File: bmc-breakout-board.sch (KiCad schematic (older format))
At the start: 26 parts, among them J1 PinHeader_2x4, J10 PinHeader_2x4, J11 PinHeader_2x05, J12 61300411121, J14 PCIE_BUS_x1, J15 0473460001, J16 PinHeader_1x07, J17 UE27AC54100, J2 PinHeader_2x13, J3 PinHeader_2x08, J4 61300411121, J5 ME1016813401101, J6 61300411121, J7 DC_SOCKET, J8 PinHeader_2x05, J9 PinHeader_1x07, Q1 BSS138AKA

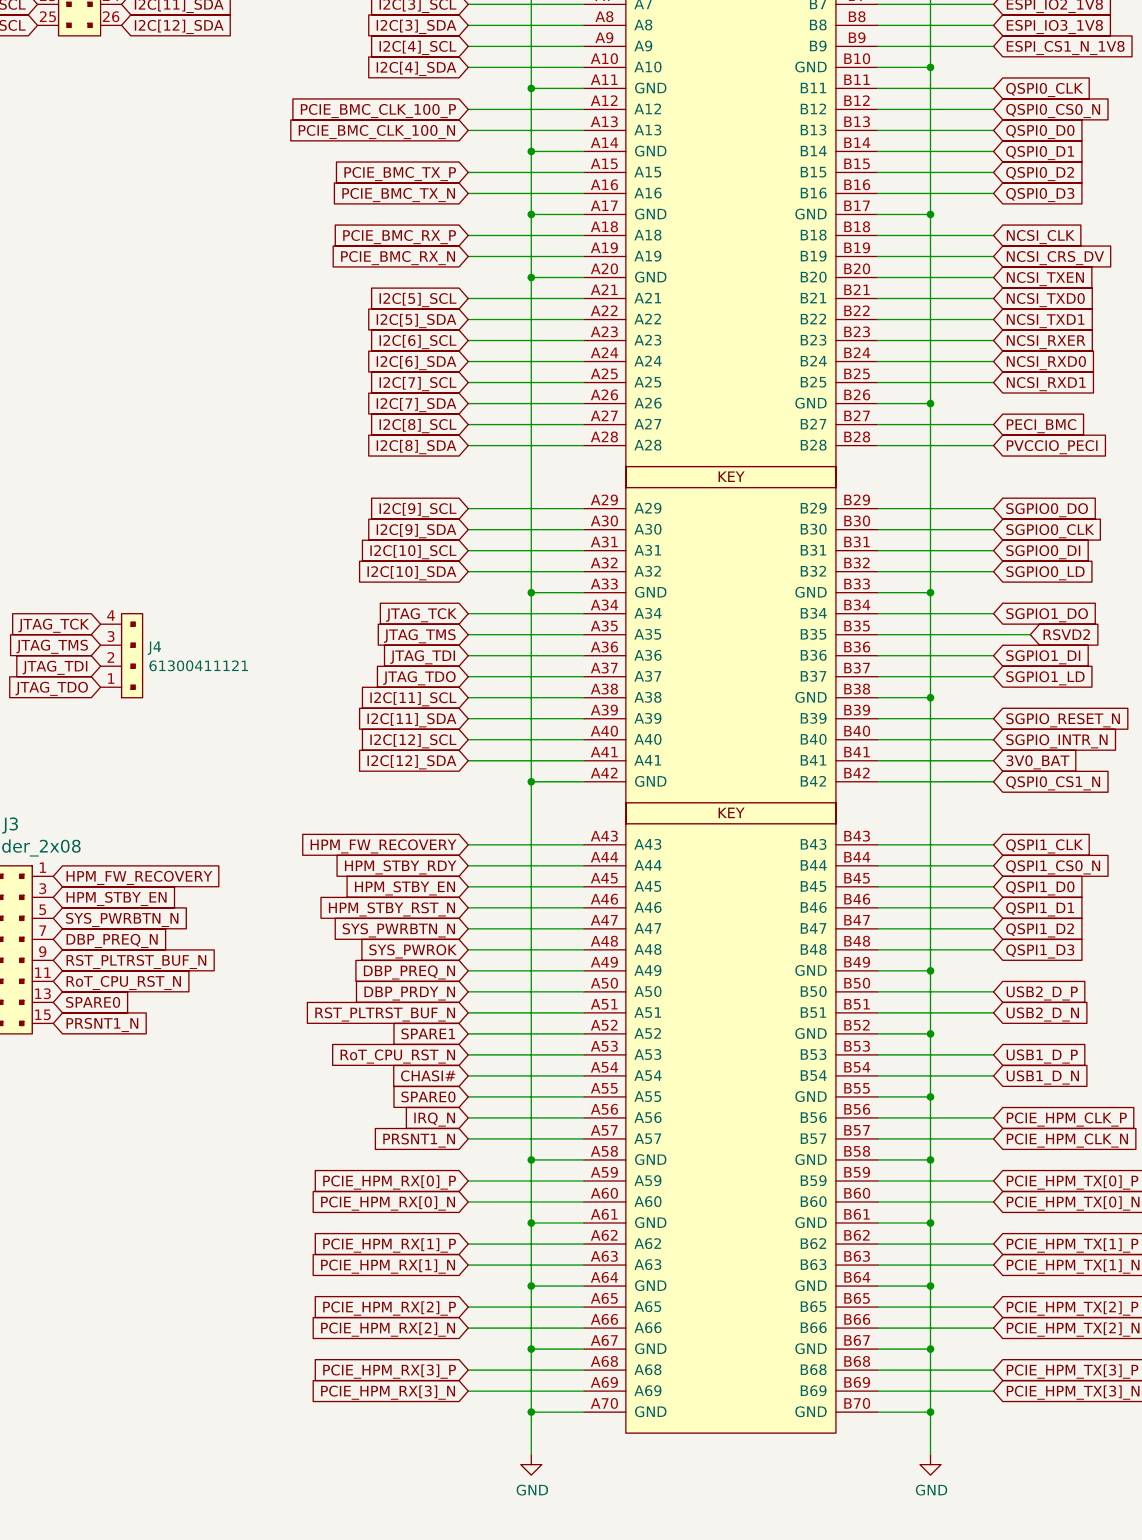
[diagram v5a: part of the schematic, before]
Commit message: Add decoupling on PCIe lines
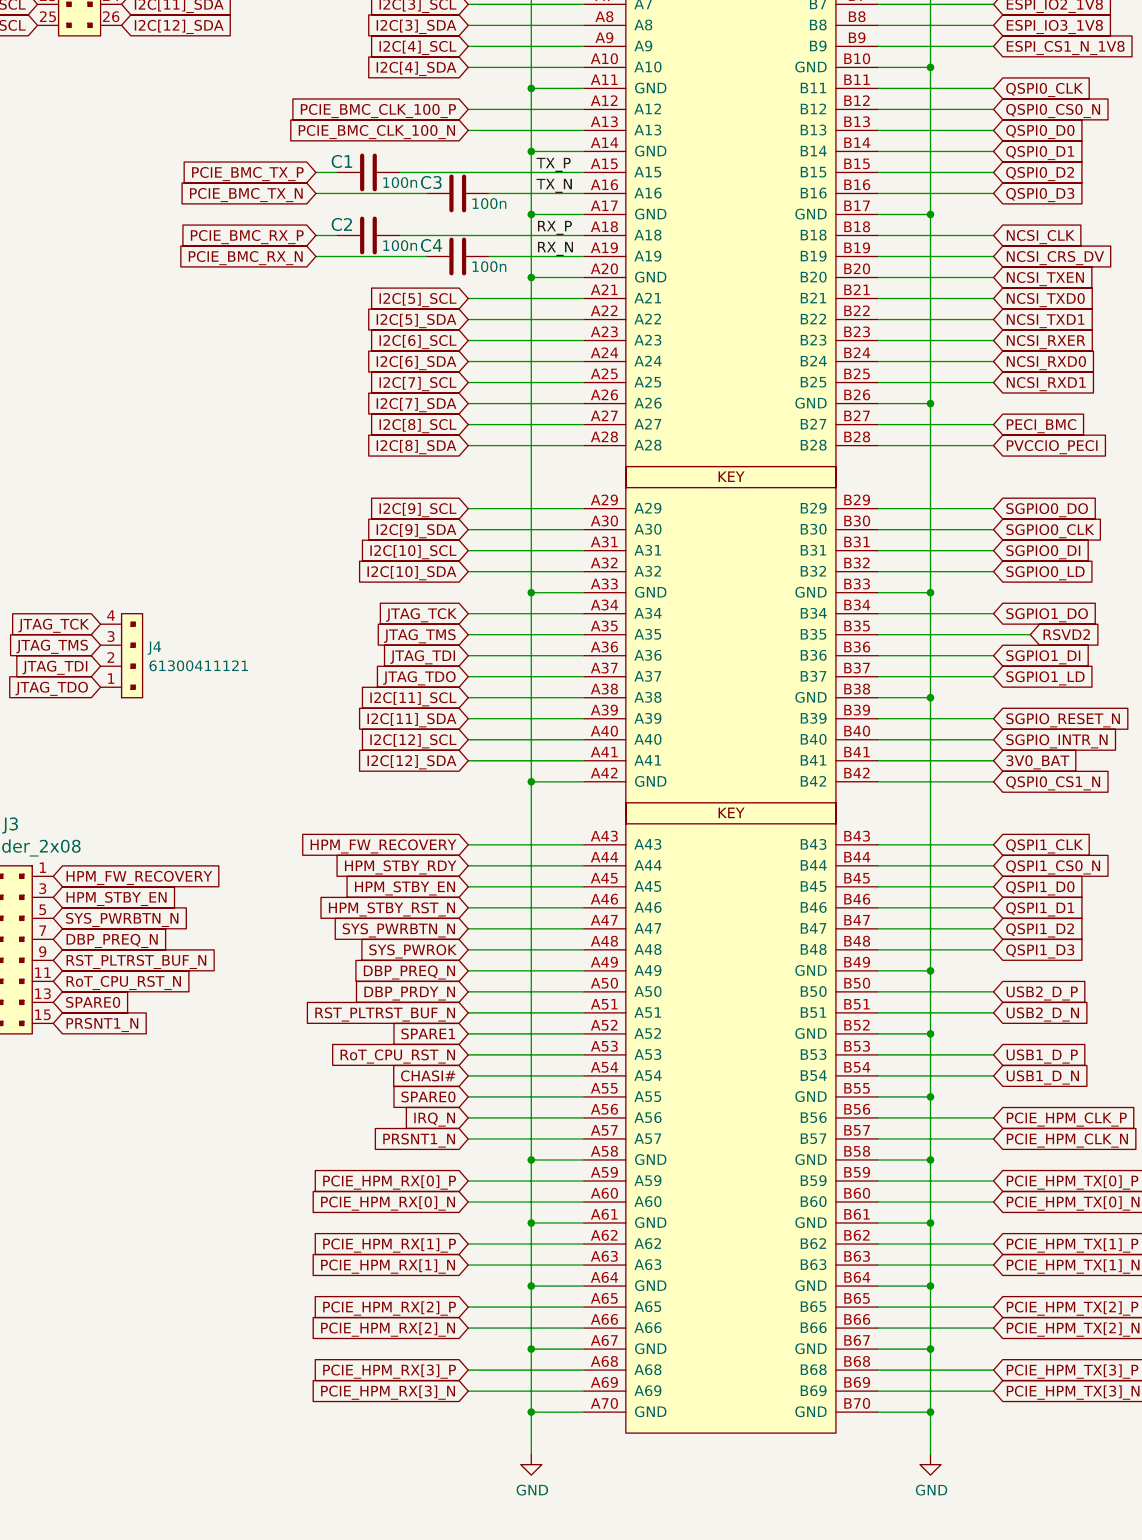
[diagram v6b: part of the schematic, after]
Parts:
- added C1, C2, C3, C4: C_100n_0402, bmc-breakout-board-footprints:0402-cap, symbol bmc-breakout-board:C_100n_0402
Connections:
- net labels added: RX_N, RX_P, TX_N, TX_P
- wire segments 290 -> 294
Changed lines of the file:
@@
 	4175 4475 3925 4475
 Wire Wire Line
-	4175 4575 3625 4575
-Wire Wire Line
-	4175 4675 3625 4675
-Wire Wire Line
-	4175 4875 3625 4875
-Wire Wire Line
-	4175 4975 3625 4975
+	4175 4675 3725 4675
+Wire Wire Line
+	4175 4875 3300 4875
+Wire Wire Line
+	4175 4975 3725 4975
 Wire Wire Line
 	4175 5175 3625 5175
@@
 	5575 8875 6125 8875
 Wire Wire Line
-	6125 9075 5575 9075
-Wire Wire Line
-	6125 9175 5575 9175
-Wire Wire Line
-	5575 9375 6125 9375
-Wire Wire Line
-	6125 9475 5575 9475
-Wire Wire Line
-	5575 9675 6125 9675
-Wire Wire Line
-	6125 9775 5575 9775
-Wire Wire Line
-	5575 9975 6125 9975
-Wire Wire Line
-	6125 10075 5575 10075
-Wire Wire Line
-	5575 10275 6125 10275
-Wire Wire Line
-	6125 10375 5575 10375
-Wire Wire Line
 	4175 7775 3625 7775
 Wire Wire Line
@@
 	4175 9275 3925 9275
 Wire Wire Line
-	3625 9375 4175 9375
-Wire Wire Line
-	4175 9475 3625 9475
-Wire Wire Line
 	4175 9575 3925 9575
 Wire Wire Line
-	3625 9675 4175 9675
-Wire Wire Line
-	4175 9775 3625 9775
-Wire Wire Line
 	4175 9875 3925 9875
 Wire Wire Line
-	3625 9975 4175 9975
-Wire Wire Line
-	4175 10075 3625 10075
-Wire Wire Line
 	4175 10175 3925 10175
-Wire Wire Line
-	3625 10275 4175 10275
-Wire Wire Line
-	4175 10375 3625 10375
 Wire Wire Line
 	4175 10475 3925 10475
@@
 Text GLabel 3625 4375 0    50   Input ~ 0
 PCIE_BMC_CLK_100_N
-Text GLabel 3625 4575 0    50   Input ~ 0
+Text GLabel 2900 4575 0    50   Input ~ 0
 PCIE_BMC_TX_P
-Text GLabel 3625 4675 0    50   Input ~ 0
+Text GLabel 2900 4675 0    50   Input ~ 0
 PCIE_BMC_TX_N
-Text GLabel 3625 4875 0    50   Input ~ 0
+Text GLabel 2900 4875 0    50   Input ~ 0
 PCIE_BMC_RX_P
-Text GLabel 3625 4975 0    50   Input ~ 0
+Text GLabel 2900 4975 0    50   Input ~ 0
 PCIE_BMC_RX_N
 Text GLabel 3625 5175 0    50   Input ~ 0
@@
 Wire Wire Line
 	5575 6275 6125 6275
-Text GLabel 3625 9375 0    50   Input ~ 0
-PCIE_HPM_RX[0]_P
-Text GLabel 3625 9475 0    50   Input ~ 0
-PCIE_HPM_RX[0]_N
-Text GLabel 3625 9675 0    50   Input ~ 0
-PCIE_HPM_RX[1]_P
-Text GLabel 3625 9775 0    50   Input ~ 0
-PCIE_HPM_RX[1]_N
-Text GLabel 3625 10275 0    50   Input ~ 0
-PCIE_HPM_RX[3]_P
-Text GLabel 3625 10375 0    50   Input ~ 0
-PCIE_HPM_RX[3]_N
 Text GLabel 6125 9675 2    50   Input ~ 0
 PCIE_HPM_TX[1]_P
@@
 Text GLabel 6125 10375 2    50   Input ~ 0
 PCIE_HPM_TX[3]_N
-Text GLabel 3625 10075 0    50   Input ~ 0
-PCIE_HPM_RX[2]_N
-Text GLabel 3625 9975 0    50   Input ~ 0
-PCIE_HPM_RX[2]_P
 Text GLabel 6125 9075 2    50   Input ~ 0
 PCIE_HPM_CLK_P
@@
 Wire Wire Line
 	10950 8900 10950 9075
+Wire Wire Line
+	5575 9075 6125 9075
+Wire Wire Line
+	5575 9175 6125 9175
+Text GLabel 3625 9975 0    50   Input ~ 0
+PCIE_HPM_RX[2]_P
+Text GLabel 3625 10075 0    50   Input ~ 0
+PCIE_HPM_RX[2]_N
+Text GLabel 3625 10375 0    50   Input ~ 0
+PCIE_HPM_RX[3]_N
+Text GLabel 3625 10275 0    50   Input ~ 0
+PCIE_HPM_RX[3]_P
+Text GLabel 3625 9775 0    50   Input ~ 0
+PCIE_HPM_RX[1]_N
+Text GLabel 3625 9675 0    50   Input ~ 0
+PCIE_HPM_RX[1]_P
+Text GLabel 3625 9475 0    50   Input ~ 0
+PCIE_HPM_RX[0]_N
+Text GLabel 3625 9375 0    50   Input ~ 0
+PCIE_HPM_RX[0]_P
+Wire Wire Line
+	4175 10375 3625 10375
+Wire Wire Line
+	3625 10275 4175 10275
+Wire Wire Line
+	4175 10075 3625 10075
+Wire Wire Line
+	3625 9975 4175 9975
+Wire Wire Line
+	4175 9775 3625 9775
+Wire Wire Line
+	3625 9675 4175 9675
+Wire Wire Line
+	4175 9475 3625 9475
+Wire Wire Line
+	3625 9375 4175 9375
+Wire Wire Line
+	5575 9475 6125 9475
+Wire Wire Line
+	5575 9375 6125 9375
+Wire Wire Line
+	5575 9775 6125 9775
+Wire Wire Line
+	5575 9675 6125 9675
+Wire Wire Line
+	5575 10075 6125 10075
+Wire Wire Line
+	5575 9975 6125 9975
+Wire Wire Line
+	5575 10375 6125 10375
+Wire Wire Line
+	5575 10275 6125 10275
+$Comp
+L bmc-breakout-board:C_100n_0402 C4
+U 1 1 610E9609
+P 3575 4975
+F 0 "C4" V 3525 4850 60  0000 C CNN
+F 1 "C_100n_0402" H 3575 4825 60  0001 C CNN
+F 2 "bmc-breakout-board-footprints:0402-cap" H 3775 5175 60  0001 L CNN
+F 3 "" H 3575 4975 50  0001 C CNN
+F 4 "Walsin" H 3775 5375 60  0001 L CNN "Manufacturer"
+F 5 "0402X104K6R3CT" H 3775 5275 60  0001 L CNN "MPN"
+F 6 "100n" V 3625 5125 50  0000 C CNN "Val"
+	1    3575 4975
+	0    1    1    0
+$EndComp
+$Comp
+L bmc-breakout-board:C_100n_0402 C2
+U 1 1 610E9600
+P 3150 4875
+F 0 "C2" V 3100 4750 60  0000 C CNN
+F 1 "C_100n_0402" H 3150 4725 60  0001 C CNN
+F 2 "bmc-breakout-board-footprints:0402-cap" H 3350 5075 60  0001 L CNN
+F 3 "" H 3150 4875 50  0001 C CNN
+F 4 "Walsin" H 3350 5275 60  0001 L CNN "Manufacturer"
+F 5 "0402X104K6R3CT" H 3350 5175 60  0001 L CNN "MPN"
+F 6 "100n" V 3200 5025 50  0000 C CNN "Val"
+	1    3150 4875
+	0    1    1    0
+$EndComp
+$Comp
+L bmc-breakout-board:C_100n_0402 C3
+U 1 1 614725A7
+P 3575 4675
+F 0 "C3" V 3525 4550 60  0000 C CNN
+F 1 "C_100n_0402" H 3575 4525 60  0001 C CNN
+F 2 "bmc-breakout-board-footprints:0402-cap" H 3775 4875 60  0001 L CNN
+F 3 "" H 3575 4675 50  0001 C CNN
+F 4 "Walsin" H 3775 5075 60  0001 L CNN "Manufacturer"
+F 5 "0402X104K6R3CT" H 3775 4975 60  0001 L CNN "MPN"
+F 6 "100n" V 3625 4825 50  0000 C CNN "Val"
+	1    3575 4675
+	0    1    1    0
+$EndComp
+$Comp
+L bmc-breakout-board:C_100n_0402 C1
+U 1 1 614725B0
+P 3150 4575
+F 0 "C1" V 3100 4450 60  0000 C CNN
+F 1 "C_100n_0402" H 3150 4425 60  0001 C CNN
+F 2 "bmc-breakout-board-footprints:0402-cap" H 3350 4775 60  0001 L CNN
+F 3 "" H 3150 4575 50  0001 C CNN
+F 4 "Walsin" H 3350 4975 60  0001 L CNN "Manufacturer"
+F 5 "0402X104K6R3CT" H 3350 4875 60  0001 L CNN "MPN"
+F 6 "100n" V 3200 4725 50  0000 C CNN "Val"
+	1    3150 4575
+	0    1    1    0
+$EndComp
+Wire Wire Line
+	4175 4575 3300 4575
+Wire Wire Line
+	3425 4675 2900 4675
+Wire Wire Line
+	3000 4575 2900 4575
+Wire Wire Line
+	3425 4975 2900 4975
+Wire Wire Line
+	3000 4875 2900 4875
+Text Label 3950 4575 0    50   ~ 0
+TX_P
+Text Label 3950 4675 0    50   ~ 0
+TX_N
+Text Label 3950 4975 0    50   ~ 0
+RX_N
+Text Label 3950 4875 0    50   ~ 0
+RX_P
 $EndSCHEMATC

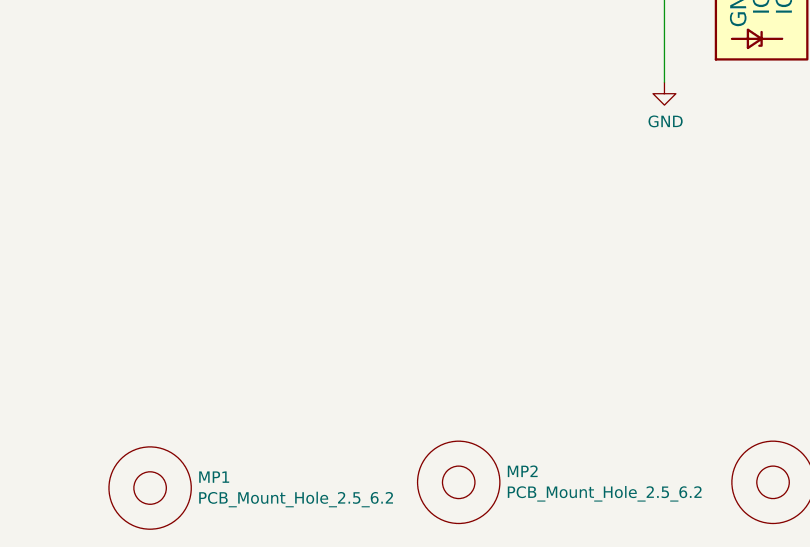
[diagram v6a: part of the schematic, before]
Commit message: Add GND probes
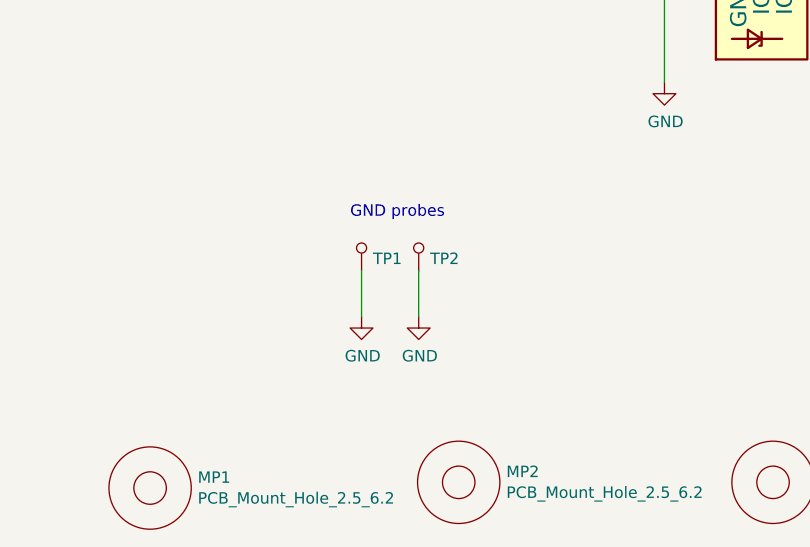
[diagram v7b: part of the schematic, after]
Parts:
- added TP1, TP2: 5001, bmc-breakout-board-footprints:Test_Point_D1.02mm, symbol bmc-breakout-board:5001
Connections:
- wire segments 294 -> 296
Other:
- note added: "GND probes"
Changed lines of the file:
@@
 Text Label 3950 4875 0    50   ~ 0
 RX_P
+$Comp
+L bmc-breakout-board:5001 TP1
+U 1 1 618E6D9F
+P 8725 9800
+F 0 "TP1" H 8675 9847 50  0000 R CNN
+F 1 "5001" H 8725 9700 50  0001 C CNN
+F 2 "bmc-breakout-board-footprints:Test_Point_D1.02mm" H 8925 10000 60  0001 L CNN
+F 3 "http://www.keyelco.com/product-pdf.cfm?p=1310" H 8925 10100 60  0001 L CNN
+F 4 "5001" H 8925 10300 60  0001 L CNN "MPN"
+F 5 "Keystone Electronics" H 8925 10900 60  0001 L CNN "Manufacturer"
+F 6 "DNP" H 8725 9800 50  0001 C CNN "DNP"
+	1    8725 9800
+	-1   0    0    1
+$EndComp
+$Comp
+L bmc-breakout-board:5001 TP2
+U 1 1 618ECEC5
+P 8975 9800
+F 0 "TP2" H 8925 9847 50  0000 R CNN
+F 1 "5001" H 8975 9700 50  0001 C CNN
+F 2 "bmc-breakout-board-footprints:Test_Point_D1.02mm" H 9175 10000 60  0001 L CNN
+F 3 "http://www.keyelco.com/product-pdf.cfm?p=1310" H 9175 10100 60  0001 L CNN
+F 4 "5001" H 9175 10300 60  0001 L CNN "MPN"
+F 5 "Keystone Electronics" H 9175 10900 60  0001 L CNN "Manufacturer"
+	1    8975 9800
+	-1   0    0    1
+$EndComp
+Wire Wire Line
+	8725 9900 8725 10100
+$Comp
+L bmc-breakout-board:GND #PWR0111
+U 1 1 61926DD1
+P 8725 10100
+F 0 "#PWR0111" H 8725 9850 50  0001 C CNN
+F 1 "GND" H 8730 9927 50  0000 C CNN
+F 2 "" H 8725 10100 50  0001 C CNN
+F 3 "" H 8725 10100 50  0001 C CNN
+	1    8725 10100
+	1    0    0    -1
+$EndComp
+Wire Wire Line
+	8975 9900 8975 10100
+$Comp
+L bmc-breakout-board:GND #PWR0112
+U 1 1 61940E5F
+P 8975 10100
+F 0 "#PWR0112" H 8975 9850 50  0001 C CNN
+F 1 "GND" H 8980 9927 50  0000 C CNN
+F 2 "" H 8975 10100 50  0001 C CNN
+F 3 "" H 8975 10100 50  0001 C CNN
+	1    8975 10100
+	1    0    0    -1
+$EndComp
+Text Notes 8675 9675 0    50   ~ 0
+GND probes
 $EndSCHEMATC

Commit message: Add FTDI schematic
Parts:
- added C? (x2): C_100n_0402, bmc-breakout-board-footprints:0402-cap, symbol bmc-breakout-board:C_100n_0402
- added C?: C_1u_0402, bmc-breakout-board-footprints:0402-cap, symbol bmc-breakout-board:C_1u_0402
- added D?: TPD2E009, bmc-breakout-board-footprints:SOT-3, symbol bmc-breakout-board:TPD2E009
- added J?: 0473460001, bmc-breakout-board-footprints:USB_Micro_B_Female_0473460001, symbol bmc-breakout-board:0473460001
- added R? (x2): R_220R_0402, bmc-breakout-board-footprints:0402-res, symbol bmc-breakout-board:R_220R_0402
- added R? (x2): R_22R_0402, bmc-breakout-board-footprints:0402-res, symbol bmc-breakout-board:R_22R_0402
- added U?: FT234XD-R, bmc-breakout-board-footprints:DFN-12-1EP_3x3mm, symbol bmc-breakout-board:FT234XD-R
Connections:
- net labels added: FTDI_USB_D_N, FTDI_USB_D_P
- wire segments 296 -> 340
- no-connect marks 15 -> 17
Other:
- note added: "TODO: Check which UART to use"
- note added: "TODO: Discuss VCC source"
- moved on the sheet: D1, D2, J14, J15, J17, J7, N1, R1, R2
